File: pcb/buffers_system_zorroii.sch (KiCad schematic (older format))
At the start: 39 parts, among them U5 74LVCH162245A

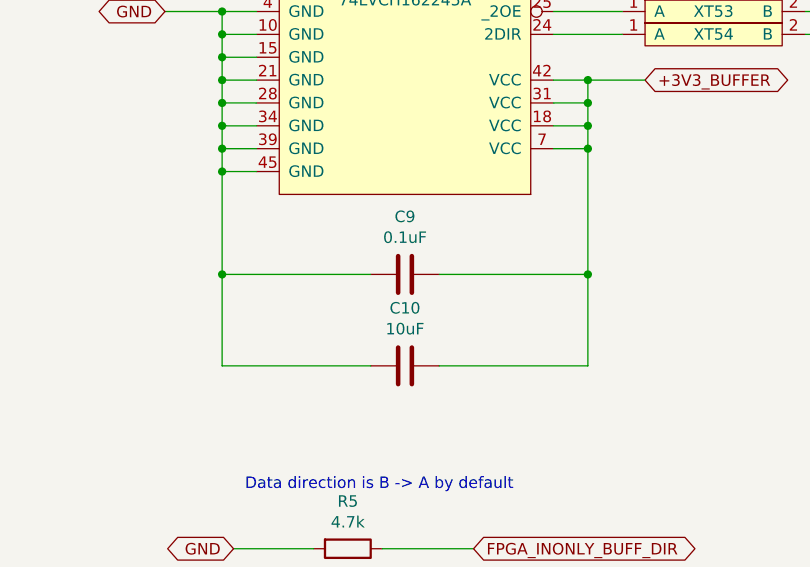
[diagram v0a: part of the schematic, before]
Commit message: more footprints assigned, caps added into open collector base circuit
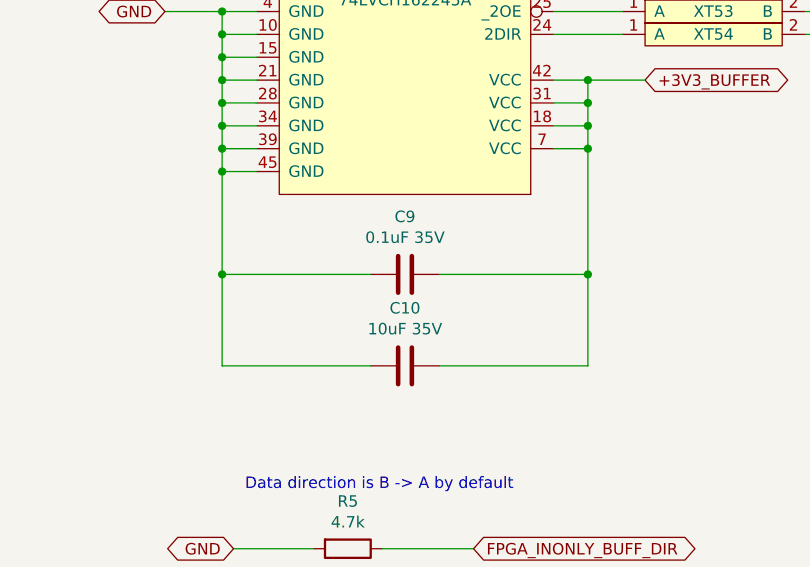
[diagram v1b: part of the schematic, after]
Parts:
- C10: value 10uF -> 10uF 35V; footprint (none) -> Capacitor_SMD:C_1210_3225Metric_Pad1.42x2.65mm_HandSolder
- C9: value 0.1uF -> 0.1uF 35V; footprint (none) -> Capacitor_SMD:C_0603_1608Metric_Pad1.05x0.95mm_HandSolder
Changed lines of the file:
@@
 P 4150 5650
 F 0 "C10" V 4402 5650 50  0000 C CNN
-F 1 "10uF" V 4311 5650 50  0000 C CNN
-F 2 "" H 4188 5500 50  0001 C CNN
+F 1 "10uF 35V" V 4311 5650 50  0000 C CNN
+F 2 "Capacitor_SMD:C_1210_3225Metric_Pad1.42x2.65mm_HandSolder" H 4188 5500 50  0001 C CNN
 F 3 "~" H 4150 5650 50  0001 C CNN
 	1    4150 5650
@@
 P 4150 5250
 F 0 "C9" V 4402 5250 50  0000 C CNN
-F 1 "0.1uF" V 4311 5250 50  0000 C CNN
-F 2 "" H 4188 5100 50  0001 C CNN
+F 1 "0.1uF 35V" V 4311 5250 50  0000 C CNN
+F 2 "Capacitor_SMD:C_0603_1608Metric_Pad1.05x0.95mm_HandSolder" H 4188 5100 50  0001 C CNN
 F 3 "~" H 4150 5250 50  0001 C CNN
 	1    4150 5250

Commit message: working on pcb 2
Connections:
- net CPUCLK_A: now also XT49.1 (A); no longer XT39.1 (A)
- net FPGA_A_BUFF_DIR: now also U5.24 (2DIR); no longer U5.1 (1DIR)
- net FPGA_CPUCLK_A: now also XT50.2 (B); no longer XT40.2 (B)
- net _BERR: now also XT47.1 (A); no longer XT37.1 (A)
- net _FPGA_A_BUFF_OE: now also U5.25 (_2OE); no longer U5.48 (_1OE)
- net _FPGA_BERR: now also XT48.2 (B); no longer XT38.2 (B)
- net _FPGA_HLT: now also XT46.2 (B); no longer XT42.2 (B)
- net _FPGA_IPL0: now also XT42.2 (B); no longer XT48.2 (B)
- net _FPGA_IPL1: now also XT40.2 (B); no longer XT46.2 (B)
- net _FPGA_IPL2: now also XT38.2 (B); no longer XT44.2 (B)
- net _FPGA_RST: now also XT44.2 (B); no longer XT50.2 (B)
- net _HLT: now also XT45.1 (A); no longer XT41.1 (A)
- net _IPL0: now also XT41.1 (A); no longer XT47.1 (A)
- net _IPL1: now also XT39.1 (A); no longer XT45.1 (A)
- net _IPL2: now also XT37.1 (A); no longer XT43.1 (A)
- net _RST: now also XT43.1 (A); no longer XT49.1 (A)
- net at XT21.2 (B): now also U5.13 (2B0); no longer U5.2 (1B0)
- net at XT23.2 (B): now also U5.14 (2B1); no longer U5.3 (1B1)
- net at XT37.2 (B): now also U5.2 (1B0); no longer U5.13 (2B0)
- net at XT39.2 (B): now also U5.3 (1B1); no longer U5.14 (2B1)
- net at XT41.2 (B): now also U5.5 (1B2); no longer U5.16 (2B2)
- net at XT43.2 (B): now also U5.6 (1B3); no longer U5.17 (2B3)
- net at XT45.2 (B): now also U5.8 (1B4); no longer U5.19 (2B4)
- net at XT47.2 (B): now also U5.9 (1B5); no longer U5.20 (2B5)
- net at XT49.2 (B): now also U5.11 (1B6); no longer U5.22 (2B6)
- net at XT51.2 (B): now also U5.12 (1B7); no longer U5.23 (2B7)
- net at XT32.1 (tp): now also U5.22 (2B6); no longer U5.11 (1B6)
- net at XT34.1 (tp): now also U5.23 (2B7); no longer U5.12 (1B7)
- net at U5.37 (1A7): now also XT52.1 (A); no longer XT36.1 (tp)
- net at U5.38 (1A6): now also XT50.1 (A); no longer XT35.1 (tp)
- net at U5.40 (1A5): now also XT48.1 (A); no longer XT33.1 (tp)
- net at U5.41 (1A4): now also XT46.1 (A); no longer XT31.1 (tp)
- net at U5.43 (1A3): now also XT44.1 (A); no longer XT29.1 (tp)
- net at U5.44 (1A2): now also XT42.1 (A); no longer XT27.1 (tp)
- net at U5.46 (1A1): now also XT40.1 (A); no longer XT25.1 (A)
- net at U5.47 (1A0): now also XT38.1 (A); no longer XT22.1 (A)
- net at XT24.1 (tp): now also U5.16 (2B2); no longer U5.5 (1B2)
- net at XT26.1 (tp): now also U5.17 (2B3); no longer U5.6 (1B3)
- net at XT28.1 (tp): now also U5.19 (2B4); no longer U5.8 (1B4)
- net at XT30.1 (tp): now also U5.20 (2B5); no longer U5.9 (1B5)
- net at XT54.1 (A): now also U5.1 (1DIR); no longer U5.24 (2DIR)
- net at XT53.1 (A): now also U5.48 (_1OE); no longer U5.25 (_2OE)
- net at U5.26 (2A7): now also XT36.1 (tp); no longer XT52.1 (A)
- net at U5.27 (2A6): now also XT35.1 (tp); no longer XT50.1 (A)
- net at U5.29 (2A5): now also XT33.1 (tp); no longer XT48.1 (A)
- net at U5.30 (2A4): now also XT31.1 (tp); no longer XT46.1 (A)
- net at U5.32 (2A3): now also XT29.1 (tp); no longer XT44.1 (A)
- net at U5.33 (2A2): now also XT27.1 (tp); no longer XT42.1 (A)
- net at U5.35 (2A1): now also XT25.1 (A); no longer XT40.1 (A)
- net at U5.36 (2A0): now also XT22.1 (A); no longer XT38.1 (A)
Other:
- moved on the sheet: XT21, XT22, XT23, XT24, XT25, XT26, XT27, XT28, XT29, XT30, XT31, XT32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

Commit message: working on pcb
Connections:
- net _FPGA_IPL1: now also XT38.2 (B); no longer XT40.2 (B)
- net _FPGA_IPL2: now also XT40.2 (B); no longer XT38.2 (B)
- net _IPL1: now also XT37.1 (A); no longer XT39.1 (A)
- net _IPL2: now also XT39.1 (A); no longer XT37.1 (A)
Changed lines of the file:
@@
 Text GLabel 2100 1750 0    50   BiDi ~ 0
 _IPL0
+Text GLabel 2100 1550 0    50   BiDi ~ 0
+_IPL1
 Text GLabel 2100 1650 0    50   BiDi ~ 0
-_IPL1
-Text GLabel 2100 1550 0    50   BiDi ~ 0
 _IPL2
 Text GLabel 2100 1850 0    50   BiDi ~ 0
@@
 Text GLabel 6100 1950 2    50   BiDi ~ 0
 _FPGA_HLT
+Text GLabel 6100 1650 2    50   BiDi ~ 0
+_FPGA_IPL2
 Text GLabel 6100 1550 2    50   BiDi ~ 0
-_FPGA_IPL2
-Text GLabel 6100 1650 2    50   BiDi ~ 0
 _FPGA_IPL1
 Text GLabel 6100 1750 2    50   BiDi ~ 0

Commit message: Board pcb updated
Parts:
- removed XT53, XT54: testpoint_cutline, WM1200:testpoint_cutline, symbol WM1200:testpoint_cutline
- C10: value 10uF 35V -> 1uF 35V; footprint Capacitor_SMD:C_1210_3225Metric_Pad1.42x2.65mm_HandSolder -> Capacitor_SMD:C_0805_2012Metric_Pad1.15x1.40mm_HandSolder
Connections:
- net FPGA_INONLY_BUFF_DIR: now also U5.1 (1DIR)
- net _FPGA_INONLY_BUFF_OE: now also U5.48 (_1OE)
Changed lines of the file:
@@
 P 4150 5650
 F 0 "C10" V 4402 5650 50  0000 C CNN
-F 1 "10uF 35V" V 4311 5650 50  0000 C CNN
-F 2 "Capacitor_SMD:C_1210_3225Metric_Pad1.42x2.65mm_HandSolder" H 4188 5500 50  0001 C CNN
+F 1 "1uF 35V" V 4311 5650 50  0000 C CNN
+F 2 "Capacitor_SMD:C_0805_2012Metric_Pad1.15x1.40mm_HandSolder" H 4188 5500 50  0001 C CNN
 F 3 "~" H 4150 5650 50  0001 C CNN
 	1    4150 5650
@@
 Wire Wire Line
 	6100 2250 5900 2250
-$Comp
-L WM1200:testpoint_cutline XT53
-U 1 1 5E93E1DE
-P 5500 2600
-F 0 "XT53" H 5500 2650 50  0000 C CNN
-F 1 "testpoint_cutline" H 5500 2750 50  0001 C CNN
-F 2 "WM1200:testpoint_cutline" H 5650 2600 50  0001 C CNN
-F 3 "" H 5650 2600 50  0001 C CNN
-	1    5500 2600
-	1    0    0    -1
-$EndComp
-$Comp
-L WM1200:testpoint_cutline XT54
-U 1 1 5E941941
-P 5500 2700
-F 0 "XT54" H 5500 2750 50  0000 C CNN
-F 1 "testpoint_cutline" H 5500 2850 50  0001 C CNN
-F 2 "WM1200:testpoint_cutline" H 5650 2700 50  0001 C CNN
-F 3 "" H 5650 2700 50  0001 C CNN
-	1    5500 2700
-	1    0    0    -1
-$EndComp
-Wire Wire Line
-	4800 2550 5100 2550
-Wire Wire Line
-	5100 2650 4800 2650
-Wire Wire Line
-	5900 2550 6100 2550
-Wire Wire Line
-	6100 2650 5900 2650
 Text GLabel 5100 4100 2    50   BiDi ~ 0
 _FPGA_A_BUFF_OE
@@
 Text GLabel 6100 2250 2    50   BiDi ~ 0
 _FPGA_KBRESET
-Text GLabel 6100 2550 2    50   BiDi ~ 0
+Text GLabel 5300 2550 2    50   BiDi ~ 0
 _FPGA_INONLY_BUFF_OE
-Text GLabel 6100 2650 2    50   BiDi ~ 0
+Text GLabel 5300 2650 2    50   BiDi ~ 0
 FPGA_INONLY_BUFF_DIR
 Text GLabel 4450 6900 2    50   BiDi ~ 0
@@
 Text GLabel 6150 3200 2    50   BiDi ~ 0
 _DSACK1
+Wire Wire Line
+	4800 2550 5300 2550
+Wire Wire Line
+	4800 2650 5300 2650
 $EndSCHEMATC

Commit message: some work on hdmi part
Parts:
- removed XT22, XT25: testpoint_cutline, WM1200:testpoint_cutline, symbol WM1200:testpoint_cutline
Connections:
- net _DSACK0: now also U5.35 (2A1)
- net _DSACK1: now also U5.36 (2A0)
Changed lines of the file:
@@
 	3150 2250 3500 2250
-$Comp
-L WM1200:testpoint_cutline XT22
-U 1 1 5E96BD33
-P 5550 3250
-F 0 "XT22" H 5550 3300 50  0000 C CNN
-F 1 "testpoint_cutline" H 5550 3400 50  0001 C CNN
-F 2 "WM1200:testpoint_cutline" H 5700 3250 50  0001 C CNN
-F 3 "" H 5700 3250 50  0001 C CNN
-	1    5550 3250
-	1    0    0    -1
-$EndComp
 $Comp
 L WM1200:testpoint XT27
@@
 F 3 "" H 5400 3450 50  0001 C CNN
 	1    5400 3450
-	1    0    0    -1
-$EndComp
-$Comp
-L WM1200:testpoint_cutline XT25
-U 1 1 5E96CD4A
-P 5550 3350
-F 0 "XT25" H 5550 3400 50  0000 C CNN
-F 1 "testpoint_cutline" H 5550 3500 50  0001 C CNN
-F 2 "WM1200:testpoint_cutline" H 5700 3350 50  0001 C CNN
-F 3 "" H 5700 3350 50  0001 C CNN
-	1    5550 3350
 	1    0    0    -1
 $EndComp
@@
 $EndComp
 Wire Wire Line
-	5150 3200 4800 3200
-Wire Wire Line
-	4800 3300 5150 3300
-Wire Wire Line
 	5150 3400 4800 3400
 Wire Wire Line
@@
 Wire Wire Line
 	4800 3900 5150 3900
-Wire Wire Line
-	5950 3200 6150 3200
-Wire Wire Line
-	6150 3300 5950 3300
-Text GLabel 6150 3300 2    50   BiDi ~ 0
+Text GLabel 5350 3300 2    50   BiDi ~ 0
 _DSACK0
-Text GLabel 6150 3200 2    50   BiDi ~ 0
+Text GLabel 5350 3200 2    50   BiDi ~ 0
 _DSACK1
 Wire Wire Line
@@
 Wire Wire Line
 	4800 2650 5300 2650
+Wire Wire Line
+	4800 3200 5350 3200
+Wire Wire Line
+	4800 3300 5350 3300
 $EndSCHEMATC

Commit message: some more work done
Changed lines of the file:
@@
 	5200 4400 4950 4400
 Connection ~ 4950 4400
-Text GLabel 6100 2050 2    50   BiDi ~ 0
+Text GLabel 6150 2050 2    50   BiDi ~ 0
 _FPGA_BERR
-Text GLabel 6100 2150 2    50   BiDi ~ 0
+Text GLabel 6150 2150 2    50   BiDi ~ 0
 FPGA_CPUCLK_A
-Text GLabel 6100 1950 2    50   BiDi ~ 0
+Text GLabel 6150 1950 2    50   BiDi ~ 0
 _FPGA_HLT
-Text GLabel 6100 1650 2    50   BiDi ~ 0
+Text GLabel 6150 1650 2    50   BiDi ~ 0
 _FPGA_IPL2
-Text GLabel 6100 1550 2    50   BiDi ~ 0
+Text GLabel 6150 1550 2    50   BiDi ~ 0
 _FPGA_IPL1
-Text GLabel 6100 1750 2    50   BiDi ~ 0
+Text GLabel 6150 1750 2    50   BiDi ~ 0
 _FPGA_IPL0
-Text GLabel 6100 1850 2    50   BiDi ~ 0
+Text GLabel 6150 1850 2    50   BiDi ~ 0
 _FPGA_RST
-Text GLabel 6100 2250 2    50   BiDi ~ 0
+Text GLabel 6150 2250 2    50   BiDi ~ 0
 _FPGA_KBRESET
 Text GLabel 5300 2550 2    50   BiDi ~ 0

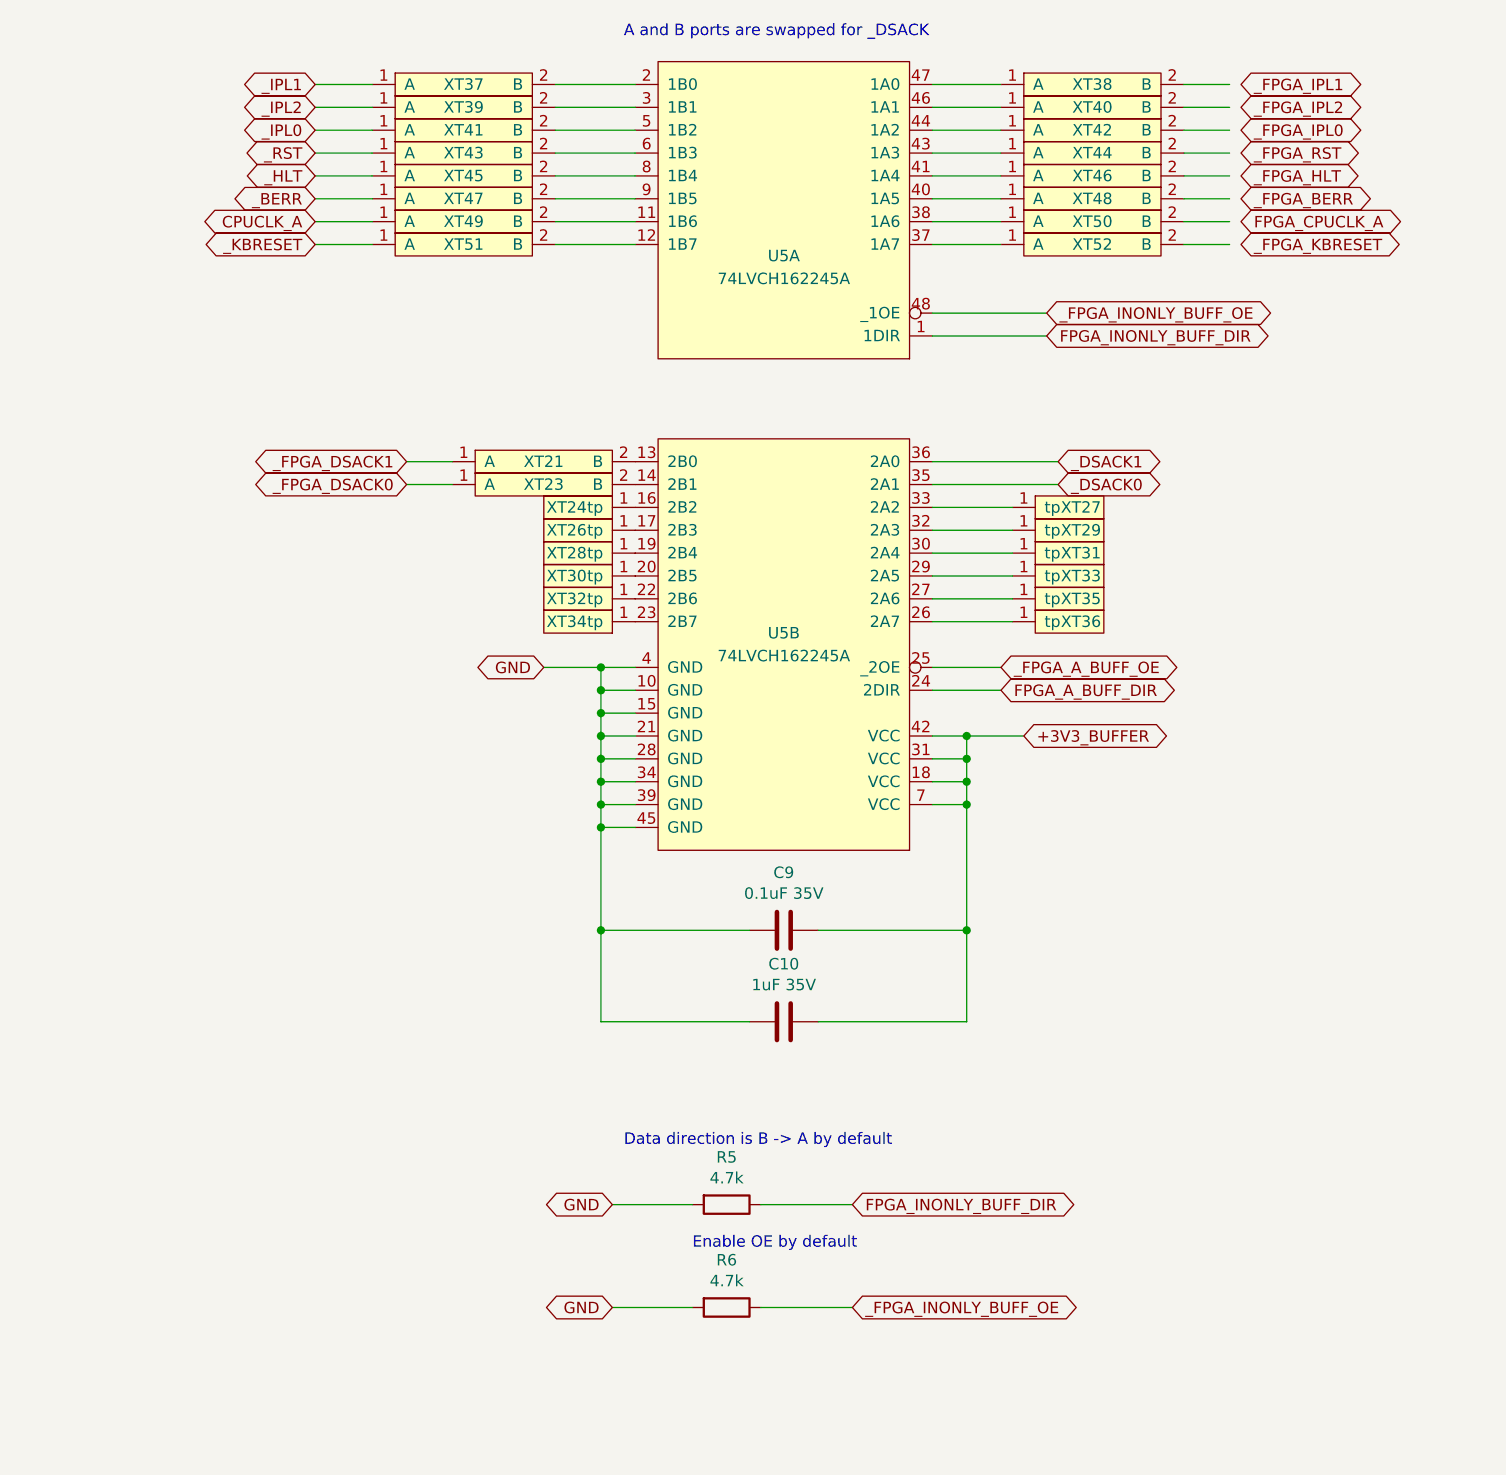
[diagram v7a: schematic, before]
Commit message: Buffers power scheme rework in progress, re-annotate board
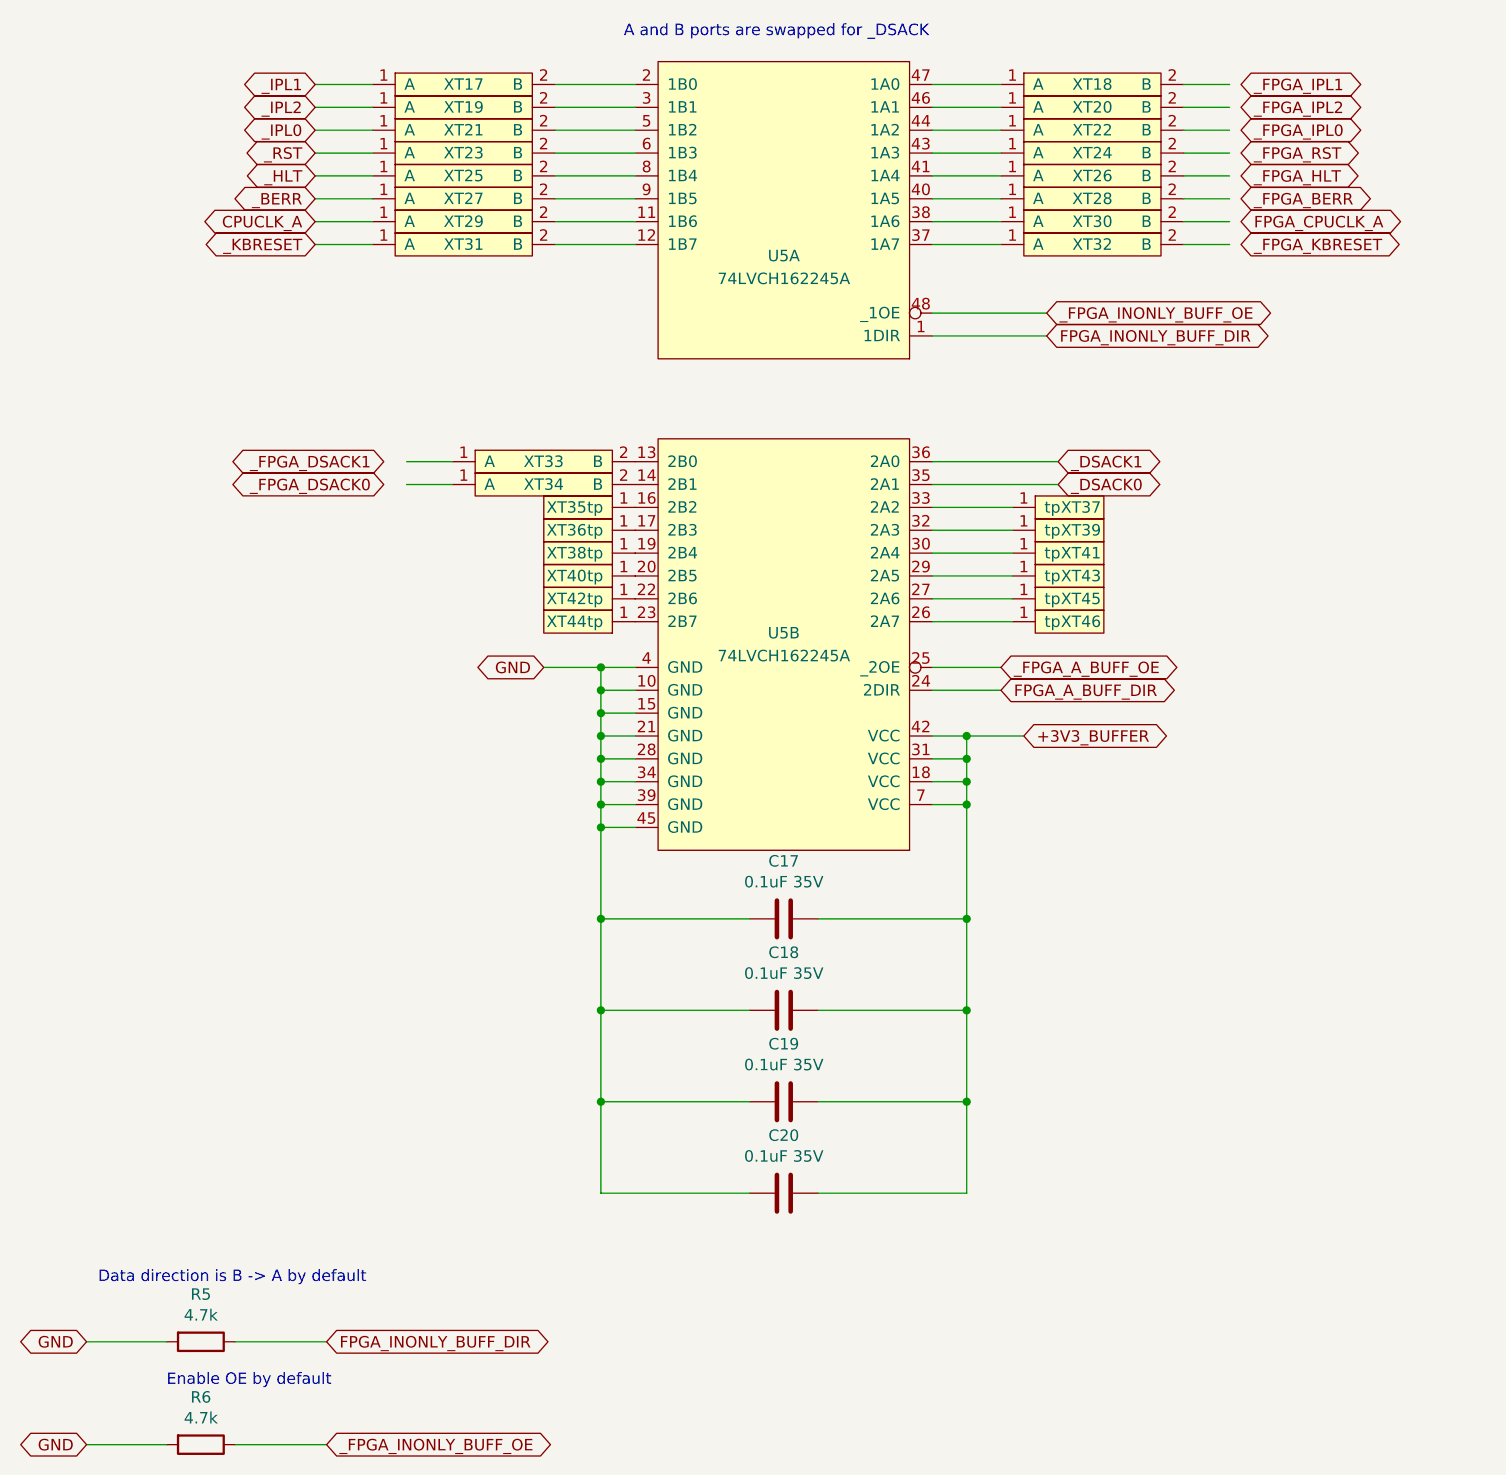
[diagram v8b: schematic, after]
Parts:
- removed C10: 1uF 35V, Capacitor_SMD:C_0805_2012Metric_Pad1.15x1.40mm_HandSolder, symbol Device:C
- removed C9: 0.1uF 35V, Capacitor_SMD:C_0603_1608Metric_Pad1.05x0.95mm_HandSolder, symbol Device:C
- added C17, C18, C19, C20: 0.1uF 35V, Capacitor_SMD:C_0603_1608Metric_Pad1.05x0.95mm_HandSolder, symbol Device:C
- renumbered XT37 to XT17, XT38 to XT18, XT39 to XT19, XT40 to XT20, XT41 to XT21, XT42 to XT22, XT43 to XT23, XT44 to XT24, XT45 to XT25, XT46 to XT26, XT47 to XT27, XT48 to XT28, XT49 to XT29, XT50 to XT30, XT51 to XT31, XT52 to XT32, XT21 to XT33, XT23 to XT34, XT24 to XT35, XT26 to XT36, XT27 to XT37, XT28 to XT38, XT29 to XT39, XT30 to XT40, XT31 to XT41, XT32 to XT42, XT33 to XT43, XT34 to XT44, XT35 to XT45, XT36 to XT46
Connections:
- wire segments 82 -> 90
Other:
- moved on the sheet: R5, R6
